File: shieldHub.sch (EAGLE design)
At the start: 7 parts

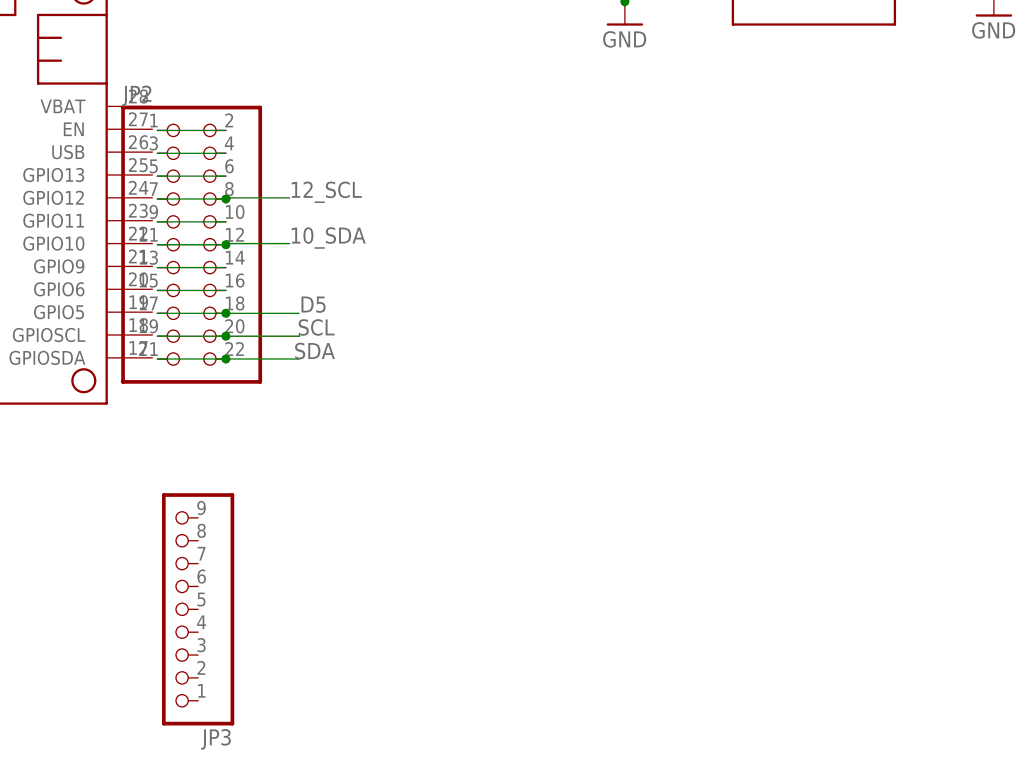
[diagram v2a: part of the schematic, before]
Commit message: Adds connector for button
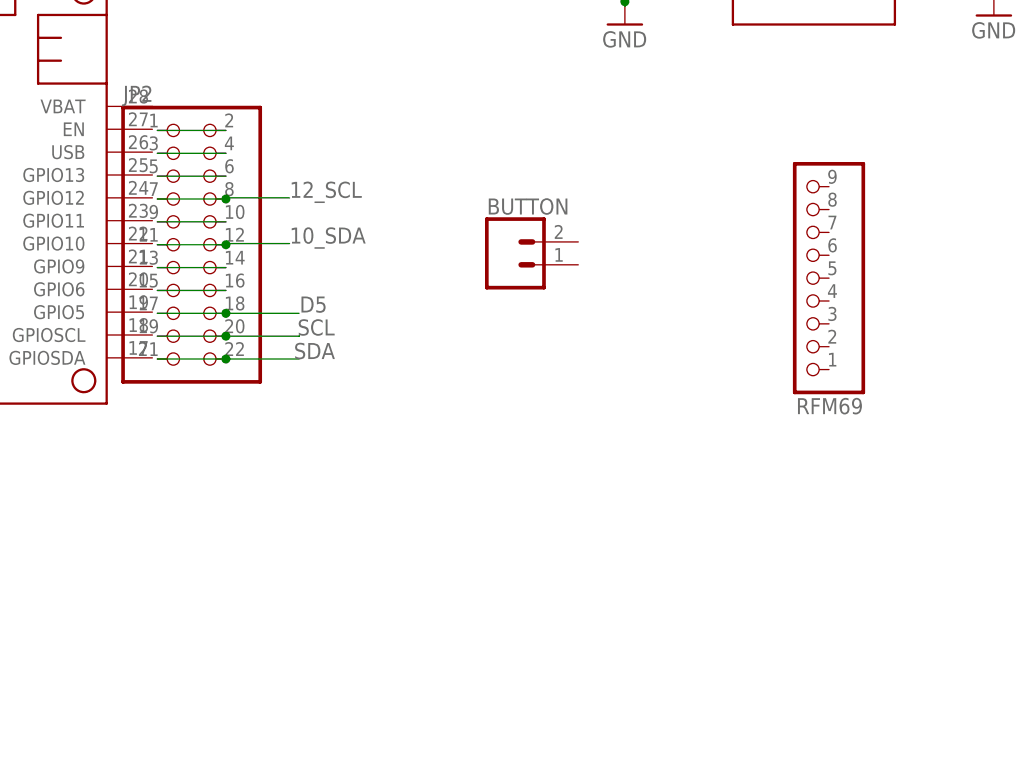
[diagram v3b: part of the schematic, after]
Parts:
- removed JP3: (no value), adafruit:PINHD-1X9
- added BUTTON: (no value), SparkFun-Connectors:CONN_023.5MM_LOCK
- added RFM69: (no value), adafruit:PINHD-1X9
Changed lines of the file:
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@@
 <part name="GND2" library="supply1" library_urn="urn:adsk.eagle:library:371" deviceset="GND" device=""/>
 <part name="MS1" library="adafruit" deviceset="FEATHERWING" device=""/>
-<part name="JP3" library="adafruit" deviceset="PINHD-1X9" device=""/>
+<part name="RFM69" library="adafruit" deviceset="PINHD-1X9" device=""/>
 <part name="VFAN" library="SparkFun-Connectors" deviceset="CONN_02" device=""/>
 <part name="GND3" library="supply1" library_urn="urn:adsk.eagle:library:371" deviceset="GND" device=""/>
+<part name="BUTTON" library="SparkFun-Connectors" deviceset="CONN_02" device="3.5MM_LOCK"/>
 </parts>
 <sheets>
@@
 </instance>
 <instance part="MS1" gate="G$1" x="25.4" y="104.14" smashed="yes" rot="R270"/>
-<instance part="JP3" gate="G$1" x="66.04" y="33.02" smashed="yes" rot="R180">
-<attribute name="NAME" x="72.39" y="19.685" size="1.778" layer="95" rot="R180"/>
-<attribute name="VALUE" x="72.39" y="48.26" size="1.778" layer="96" rot="R180"/>
+<instance part="RFM69" gate="G$1" x="136.14" y="69.82" smashed="yes" rot="R180">
+<attribute name="NAME" x="142.49" y="56.485" size="1.778" layer="95" rot="R180"/>
+<attribute name="VALUE" x="142.49" y="85.06" size="1.778" layer="96" rot="R180"/>
 </instance>
 <instance part="VFAN" gate="G$1" x="177.62" y="110" smashed="yes" rot="R180">
@@
 <attribute name="VALUE" x="163.96" y="99.26" size="1.778" layer="96"/>
 </instance>
+<instance part="BUTTON" gate="G$1" x="103.2" y="71.3" smashed="yes">
+<attribute name="VALUE" x="100.66" y="66.474" size="1.778" layer="96" font="vector"/>
+<attribute name="NAME" x="100.66" y="76.888" size="1.778" layer="95" font="vector"/>
+</instance>
 </instances>

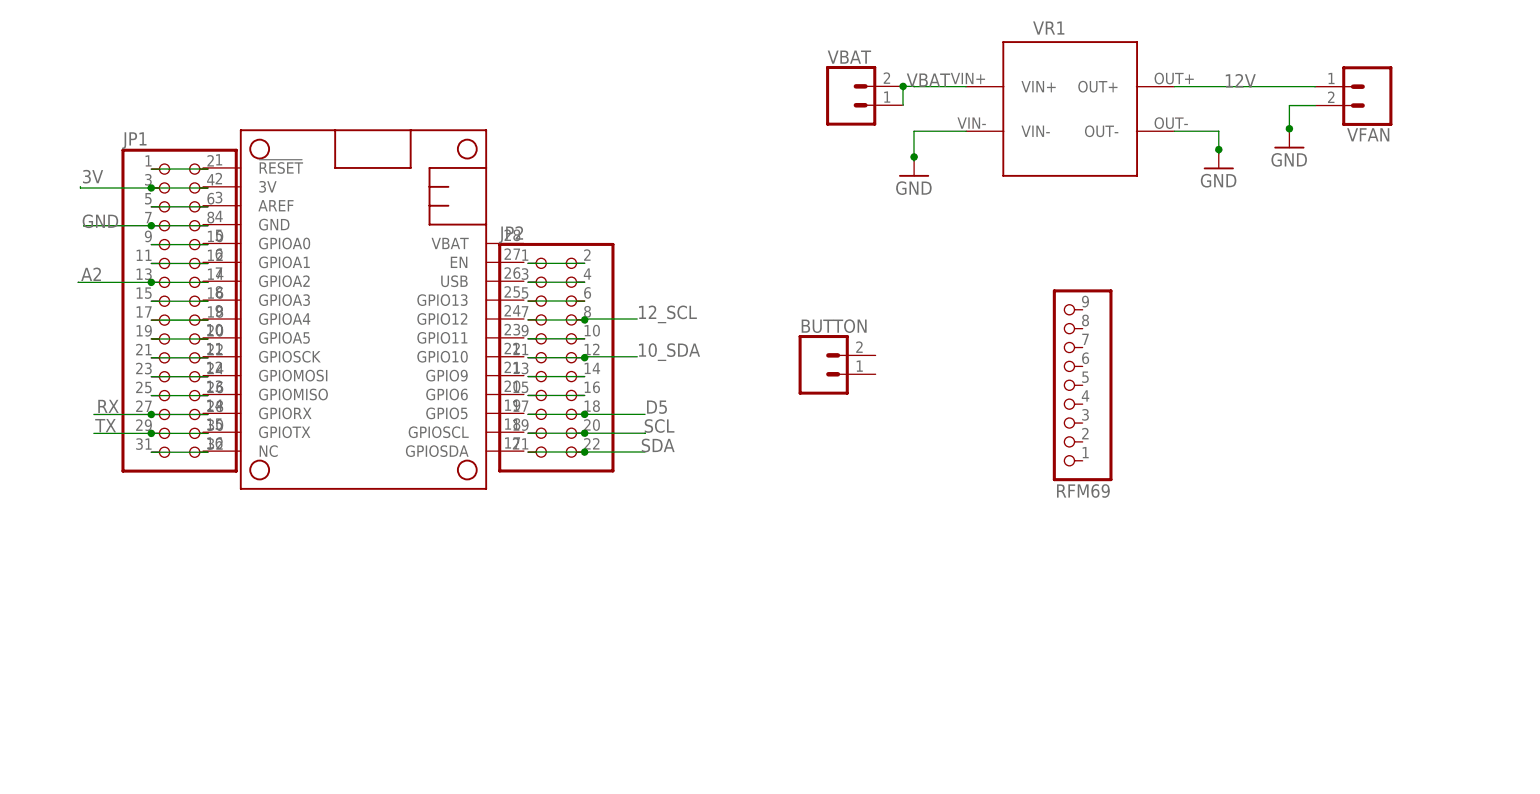
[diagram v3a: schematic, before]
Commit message: Connects rfm69 to boron
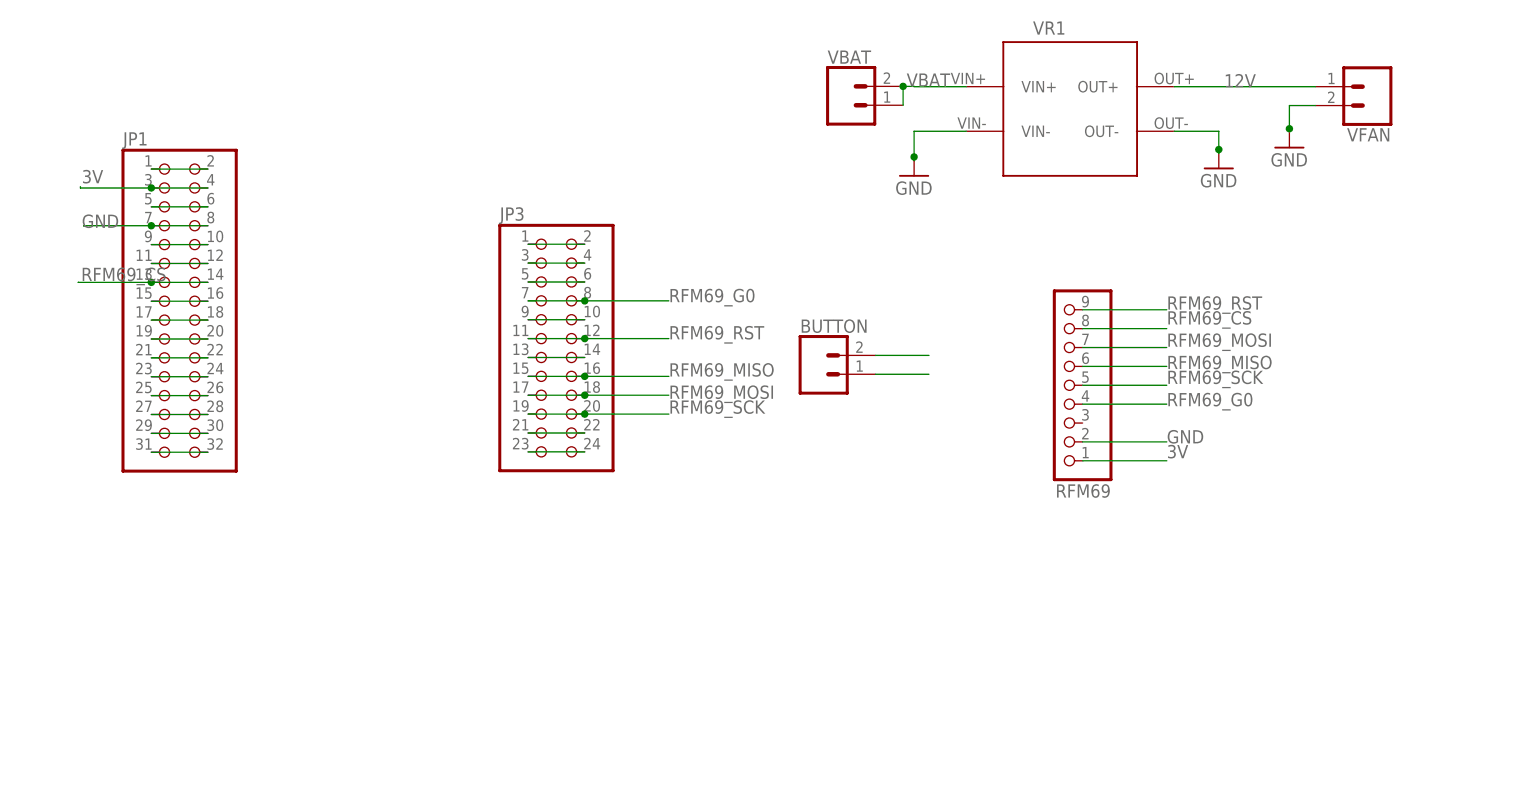
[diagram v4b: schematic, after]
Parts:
- removed JP2: (no value), pinhead:PINHD-2X11
- removed MS1: FEATHERWING, adafruit:FEATHERWING
- added JP3: (no value), pinhead:PINHD-2X12
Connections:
- removed net 10_SDA: JP2.11, JP2.12
- removed net 12_SCL: JP2.7, JP2.8
- removed net A2: JP1.13, JP1.14
- removed net D5: JP2.17, JP2.18
- removed net N$17: JP2.1, JP2.2
- removed net N$18: JP2.3, JP2.4
- removed net SCL: JP2.19, JP2.20
- removed net SDA: JP2.21, JP2.22
- new net N$14: JP3.21, JP3.22
- new net N$2: BUTTON.2
- new net N$25: JP3.1, JP3.2
- new net N$4: BUTTON.1
- new net N$7: JP3.23, JP3.24
- new net RFM69_CS: JP1.13, JP1.14, RFM69.8
- new net RFM69_G0: JP3.7, JP3.8, RFM69.4
- new net RFM69_MISO: JP3.15, JP3.16, RFM69.6
- new net RFM69_MOSI: JP3.17, JP3.18, RFM69.7
- new net RFM69_RST: JP3.11, JP3.12, RFM69.9
- new net RFM69_SCK: JP3.19, JP3.20, RFM69.5
- net 3V: now also RFM69.1
- net GND: now also RFM69.2
- net N$19: now also JP3.13, JP3.14; no longer JP2.5, JP2.6
- net N$21: now also JP3.10, JP3.9; no longer JP2.10, JP2.9
- net N$23: now also JP3.5, JP3.6; no longer JP2.13, JP2.14
- net N$24: now also JP3.3, JP3.4; no longer JP2.15, JP2.16

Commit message: Connects button to boron
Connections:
- removed net N$2: BUTTON.2
- removed net N$4: BUTTON.1
- removed net N$9: JP1.17, JP1.18
- new net IRR_BUTT: BUTTON.1, JP1.17, JP1.18
- net GND: now also BUTTON.2
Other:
- moved on the sheet: BUTTON
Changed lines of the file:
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@@
 <part name="BUTTON" library="SparkFun-Connectors" deviceset="CONN_02" device="3.5MM_LOCK"/>
 <part name="JP3" library="pinhead" library_urn="urn:adsk.eagle:library:325" deviceset="PINHD-2X12" device="" package3d_urn="urn:adsk.eagle:package:22420/2"/>
+<part name="GND4" library="supply1" library_urn="urn:adsk.eagle:library:371" deviceset="GND" device=""/>
 </parts>
 <sheets>
@@
 <attribute name="VALUE" x="163.96" y="99.26" size="1.778" layer="96"/>
 </instance>
-<instance part="BUTTON" gate="G$1" x="103.2" y="71.3" smashed="yes">
-<attribute name="VALUE" x="100.66" y="66.474" size="1.778" layer="96" font="vector"/>
-<attribute name="NAME" x="100.66" y="76.888" size="1.778" layer="95" font="vector"/>
+<instance part="BUTTON" gate="G$1" x="118.2" y="52.3" smashed="yes" rot="R180">
+<attribute name="VALUE" x="120.74" y="57.126" size="1.778" layer="96" font="vector" rot="R180"/>
+<attribute name="NAME" x="120.74" y="46.712" size="1.778" layer="95" font="vector" rot="R180"/>
 </instance>
 <instance part="JP3" gate="A" x="66.6" y="76.1" smashed="yes">
 <attribute name="NAME" x="60.25" y="91.975" size="1.778" layer="95"/>
 <attribute name="VALUE" x="60.25" y="55.78" size="1.778" layer="96"/>
+</instance>
+<instance part="GND4" gate="1" x="107" y="43" smashed="yes">
+<attribute name="VALUE" x="104.46" y="40.46" size="1.778" layer="96"/>
 </instance>
 </instances>
@@
 <label x="150" y="62" size="1.778" layer="95"/>
 </segment>
+<segment>
+<pinref part="BUTTON" gate="G$1" pin="2"/>
+<wire x1="110.58" y1="49.76" x2="107" y2="49.76" width="0.1524" layer="91"/>
+<wire x1="107" y1="49.76" x2="107" y2="45.54" width="0.1524" layer="91"/>
+<pinref part="GND4" gate="1" pin="GND"/>
+<wire x1="107" y1="45.54" x2="107" y2="45" width="0.1524" layer="91"/>
+<junction x="107" y="45.54"/>
+</segment>
 </net>
 <net name="N$5" class="0">
@@
 </segment>
 </net>
-<net name="N$9" class="0">
+<net name="IRR_BUTT" class="0">
 <segment>
 <pinref part="JP1" gate="A" pin="17"/>
 <pinref part="JP1" gate="A" pin="18"/>
 <wire x1="13.36" y1="78.59" x2="20.98" y2="78.59" width="0.1524" layer="91"/>
+<wire x1="13.36" y1="78.59" x2="-5" y2="78.59" width="0.1524" layer="91"/>
+<junction x="13.36" y="78.59"/>
+<label x="-5" y="79" size="1.778" layer="95"/>
+</segment>
+<segment>
+<pinref part="BUTTON" gate="G$1" pin="1"/>
+<wire x1="110.58" y1="52.3" x2="98" y2="52.3" width="0.1524" layer="91"/>
+<label x="98" y="53" size="1.778" layer="95"/>
 </segment>
 </net>
@@
 <pinref part="JP1" gate="A" pin="14"/>
 <wire x1="13.36" y1="83.67" x2="20.98" y2="83.67" width="0.1524" layer="91"/>
-<wire x1="13.36" y1="83.67" x2="3.53" y2="83.67" width="0.1524" layer="91"/>
-<wire x1="3.53" y1="83.67" x2="3.53" y2="83.68" width="0.1524" layer="91"/>
 <junction x="13.36" y="83.67"/>
-<label x="3.91" y="83.85" size="1.778" layer="95"/>
+<wire x1="13.36" y1="83.67" x2="-5" y2="83.67" width="0.1524" layer="91"/>
+<label x="-5" y="84" size="1.778" layer="95"/>
 </segment>
 </net>
@@
 </segment>
 </net>
-<net name="N$2" class="0">
-<segment>
-<pinref part="BUTTON" gate="G$1" pin="2"/>
-<wire x1="110.82" y1="73.84" x2="118" y2="73.84" width="0.1524" layer="91"/>
-</segment>
-</net>
-<net name="N$4" class="0">
-<segment>
-<pinref part="BUTTON" gate="G$1" pin="1"/>
-<wire x1="110.82" y1="71.3" x2="118" y2="71.3" width="0.1524" layer="91"/>
-</segment>
-</net>

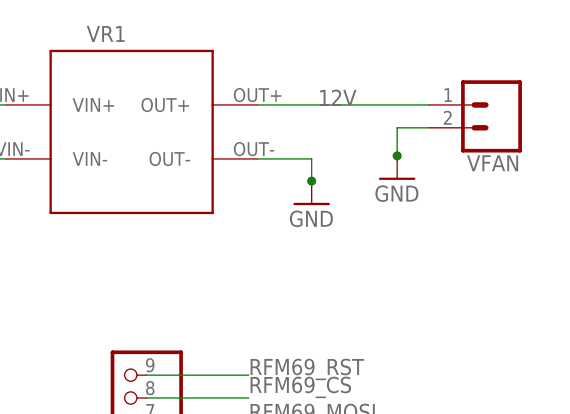
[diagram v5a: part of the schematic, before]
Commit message: Replaces fan power header pin with a connector pin
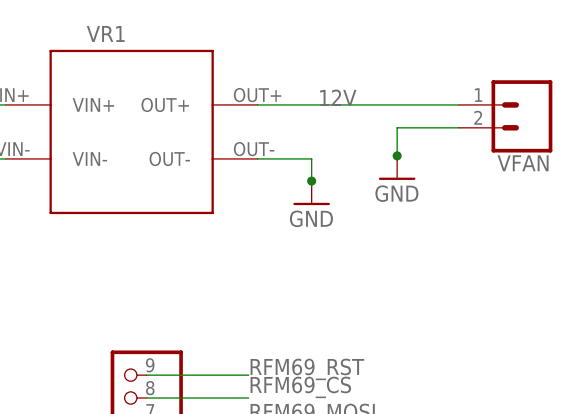
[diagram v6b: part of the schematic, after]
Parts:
- VFAN: device SparkFun-Connectors:CONN_02 -> SparkFun-Connectors:CONN_023.5MM_LOCK
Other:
- moved on the sheet: VFAN
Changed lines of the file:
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@@
 <setting verticaltext="up"/>
 </settings>
-<grid distance="1" unitdist="mm" unit="mm" style="dots" multiple="1" display="yes" altdistance="1" altunitdist="mm" altunit="mm"/>
+<grid distance="0.1" unitdist="mm" unit="mm" style="dots" multiple="1" display="yes" altdistance="1" altunitdist="mm" altunit="mm"/>
 <layers>
 <layer number="1" name="Top" color="4" fill="1" visible="no" active="no"/>
@@
 <part name="GND2" library="supply1" library_urn="urn:adsk.eagle:library:371" deviceset="GND" device=""/>
 <part name="RFM69" library="adafruit" deviceset="PINHD-1X9" device=""/>
-<part name="VFAN" library="SparkFun-Connectors" deviceset="CONN_02" device=""/>
 <part name="GND3" library="supply1" library_urn="urn:adsk.eagle:library:371" deviceset="GND" device=""/>
 <part name="BUTTON" library="SparkFun-Connectors" deviceset="CONN_02" device="3.5MM_LOCK"/>
 <part name="JP3" library="pinhead" library_urn="urn:adsk.eagle:library:325" deviceset="PINHD-2X12" device="" package3d_urn="urn:adsk.eagle:package:22420/2"/>
 <part name="GND4" library="supply1" library_urn="urn:adsk.eagle:library:371" deviceset="GND" device=""/>
+<part name="VFAN" library="SparkFun-Connectors" deviceset="CONN_02" device="3.5MM_LOCK"/>
 </parts>
 <sheets>
@@
 <attribute name="VALUE" x="142.49" y="85.06" size="1.778" layer="96" rot="R180"/>
 </instance>
-<instance part="VFAN" gate="G$1" x="177.62" y="110" smashed="yes" rot="R180">
-<attribute name="VALUE" x="180.16" y="114.826" size="1.778" layer="96" font="vector" rot="R180"/>
-<attribute name="NAME" x="180.16" y="104.412" size="1.778" layer="95" font="vector" rot="R180"/>
-</instance>
 <instance part="GND3" gate="1" x="166.5" y="101.8" smashed="yes">
 <attribute name="VALUE" x="163.96" y="99.26" size="1.778" layer="96"/>
@@
 <instance part="GND4" gate="1" x="107" y="43" smashed="yes">
 <attribute name="VALUE" x="104.46" y="40.46" size="1.778" layer="96"/>
+</instance>
+<instance part="VFAN" gate="G$1" x="181" y="110" smashed="yes" rot="R180">
+<attribute name="VALUE" x="183.54" y="114.826" size="1.778" layer="96" font="vector" rot="R180"/>
+<attribute name="NAME" x="183.54" y="104.412" size="1.778" layer="95" font="vector" rot="R180"/>
 </instance>
 </instances>
@@
 </segment>
 <segment>
-<pinref part="VFAN" gate="G$1" pin="2"/>
-<wire x1="170" y1="107.46" x2="166.5" y2="107.46" width="0.1524" layer="91"/>
-<wire x1="166.5" y1="107.46" x2="166.5" y2="104.34" width="0.1524" layer="91"/>
 <wire x1="166.5" y1="104.34" x2="166.5" y2="104.2" width="0.1524" layer="91"/>
 <wire x1="166.5" y1="104.2" x2="166.4" y2="104.2" width="0.1524" layer="91"/>
 <pinref part="GND3" gate="1" pin="GND"/>
+<pinref part="VFAN" gate="G$1" pin="2"/>
+<wire x1="166.5" y1="104.34" x2="166.5" y2="107.46" width="0.1524" layer="91"/>
+<wire x1="166.5" y1="107.46" x2="173.38" y2="107.46" width="0.1524" layer="91"/>
 <junction x="166.5" y="104.34"/>
 </segment>
@@
 <segment>
 <pinref part="VR1" gate="G$1" pin="OUT+"/>
+<wire x1="151" y1="110" x2="173.38" y2="110" width="0.1524" layer="91"/>
+<label x="157.7" y="109.9" size="1.778" layer="95"/>
 <pinref part="VFAN" gate="G$1" pin="1"/>
-<wire x1="151" y1="110" x2="170" y2="110" width="0.1524" layer="91"/>
-<label x="157.7" y="109.9" size="1.778" layer="95"/>
-</segment>
-</net>
+</segment>
+</net>
